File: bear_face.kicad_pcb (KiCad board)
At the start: 2 copper layers, 301.7 x 112.6 mm, 190 parts, among them J1 USB_B_Micro, SW1 SW_Push, U1 ATmega32U4-AU, Y1 16MHz

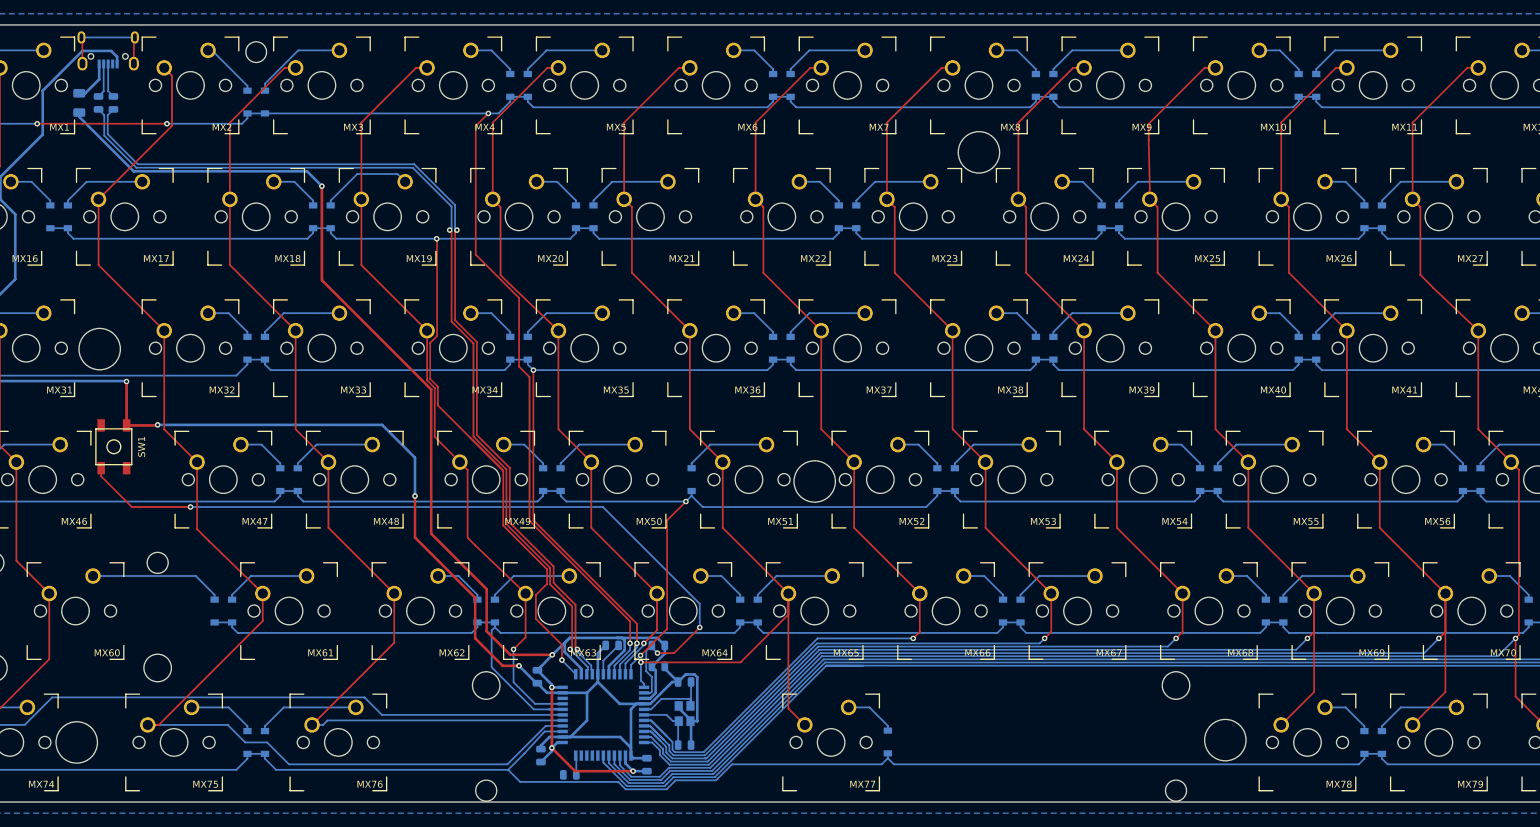
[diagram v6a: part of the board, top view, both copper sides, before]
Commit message: Load caps moved closer, minor MCU track tweaks, USB-Micro changed to molex
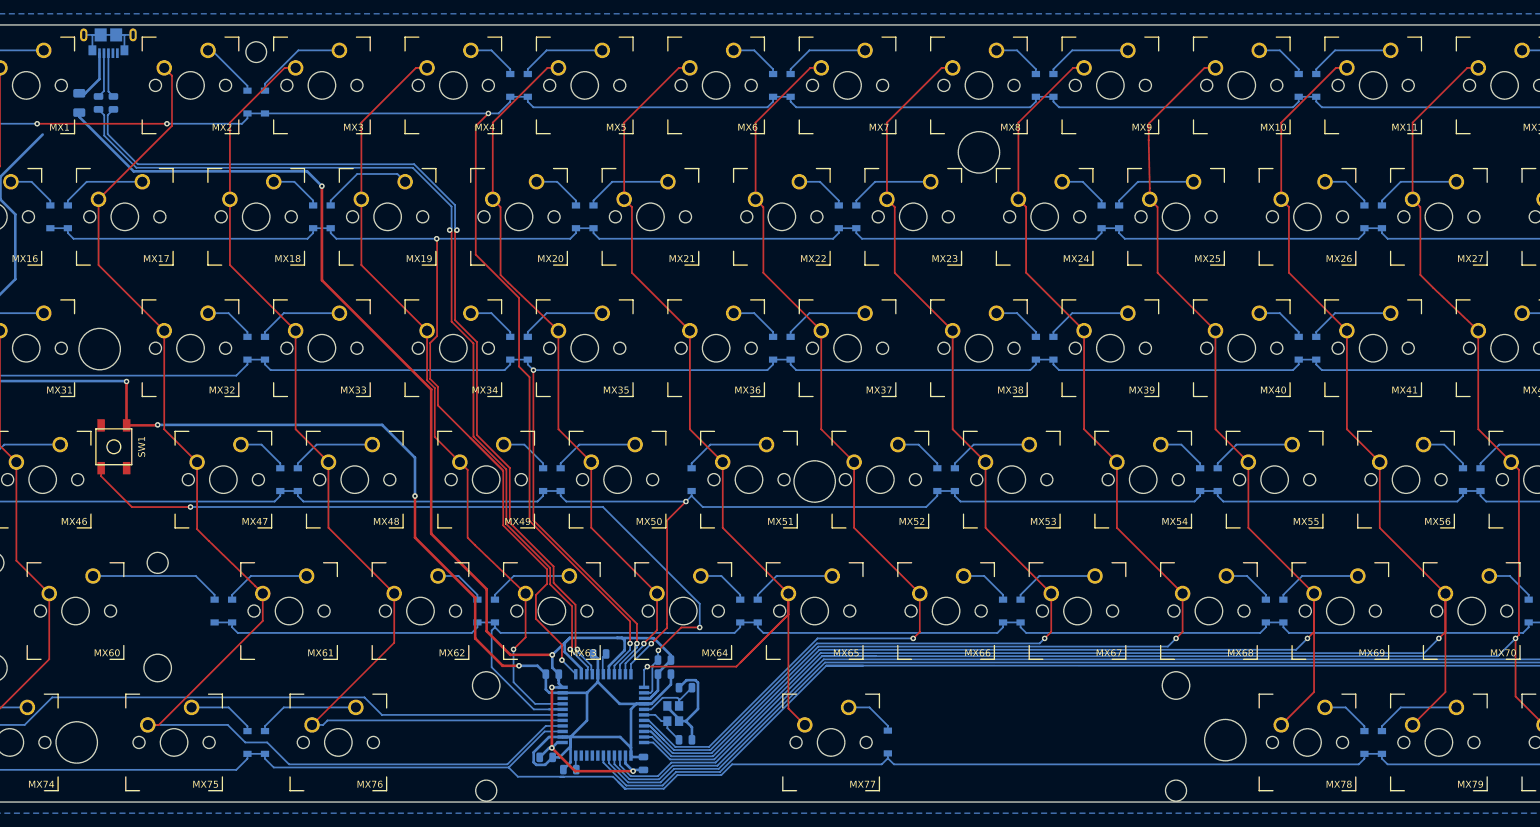
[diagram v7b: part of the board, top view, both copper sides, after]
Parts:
- J1: footprint Connector_USB:USB_Micro-B_Wuerth_629105150521 -> Connector_USB:USB_Micro-B_GCT_USB3076-30-A
- moved R1 2.31 mm to (164.7, 161.2)
- moved C3 2.19 mm to (155.3, 160.3)
- moved C7 2.19 mm to (148.5, 163.2), turned to 180 degrees
- moved Y1 1.65 mm to (166.0, 168.9)
- moved C5 1.42 mm to (164.7, 163.2)
- moved J1 1.12 mm to (84.1, 71.7)
- moved C2 0.84 mm to (167.8, 165.2)
- moved C6 0.80 mm to (147.6, 175.3), turned to 0 degrees
- moved C1 0.77 mm to (167.8, 172.7)
- moved R4 0.76 mm to (151.0, 177.0)
- moved C4 0.54 mm to (161.7, 176.1)
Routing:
- net COL5: track 142.1 -> 150.6 mm
- net GND: track 262.3 -> 253.8 mm
- net COL11: track 248.8 -> 256.5 mm
- net COL6: track 149.5 -> 145.0 mm
- net Net-(R1-Pad2): track 116.8 -> 114.0 mm
- net Net-(C3-Pad1): track 5.09 -> 3.17 mm
- net Net-(J1-Pad6): track 15.7 -> 13.9 mm
- net Net-(C1-Pad1): track 8.91 -> 7.16 mm
- net ROW5: track 306.8 -> 308.5 mm
- net Net-(C2-Pad1): track 11.9 -> 10.2 mm
- net VCC: track 5.95 -> 7.54 mm
- net D-: track 5.02 -> 6.60 mm
- net D+: track 5.02 -> 6.57 mm
- net COL8: track 186.2 -> 185.1 mm
- net COL7: track 168.8 -> 167.7 mm
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
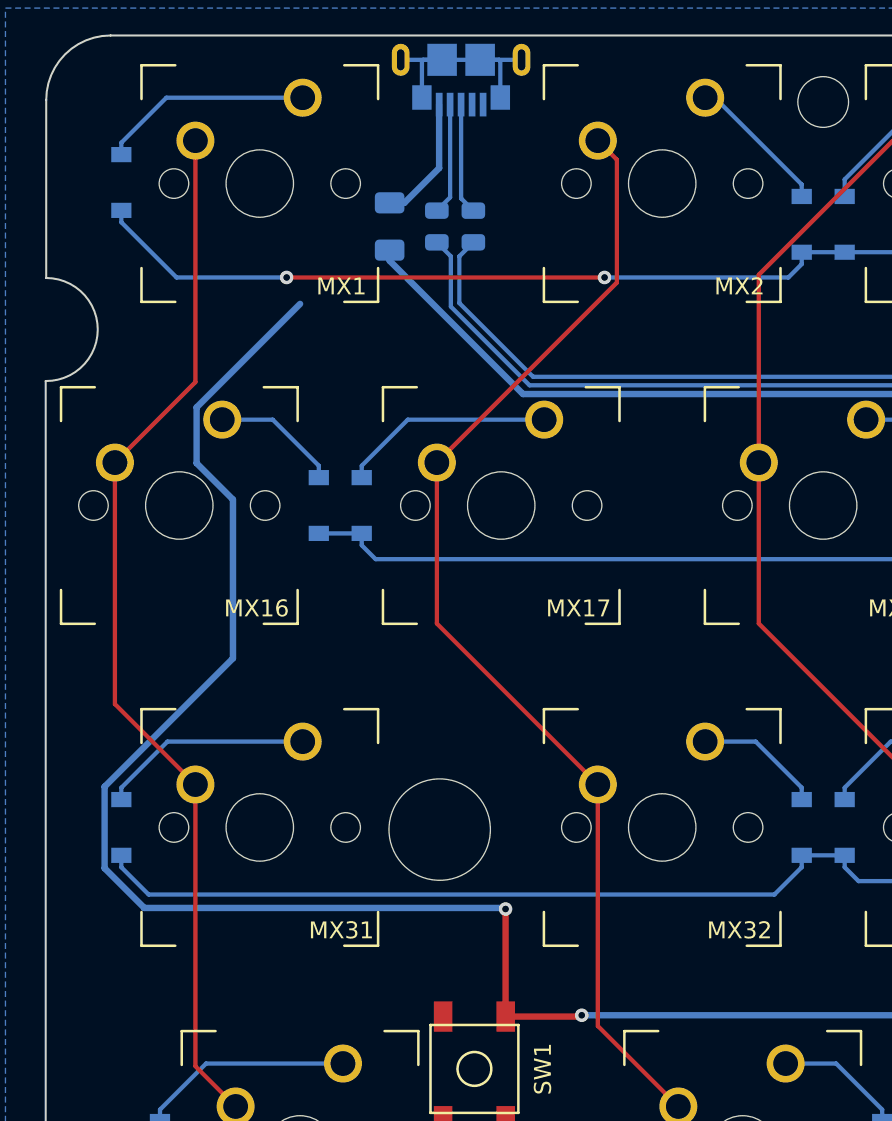
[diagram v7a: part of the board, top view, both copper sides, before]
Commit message: Reconnected USB GND to SW1
Minor tracking tweaks, DRC check passed
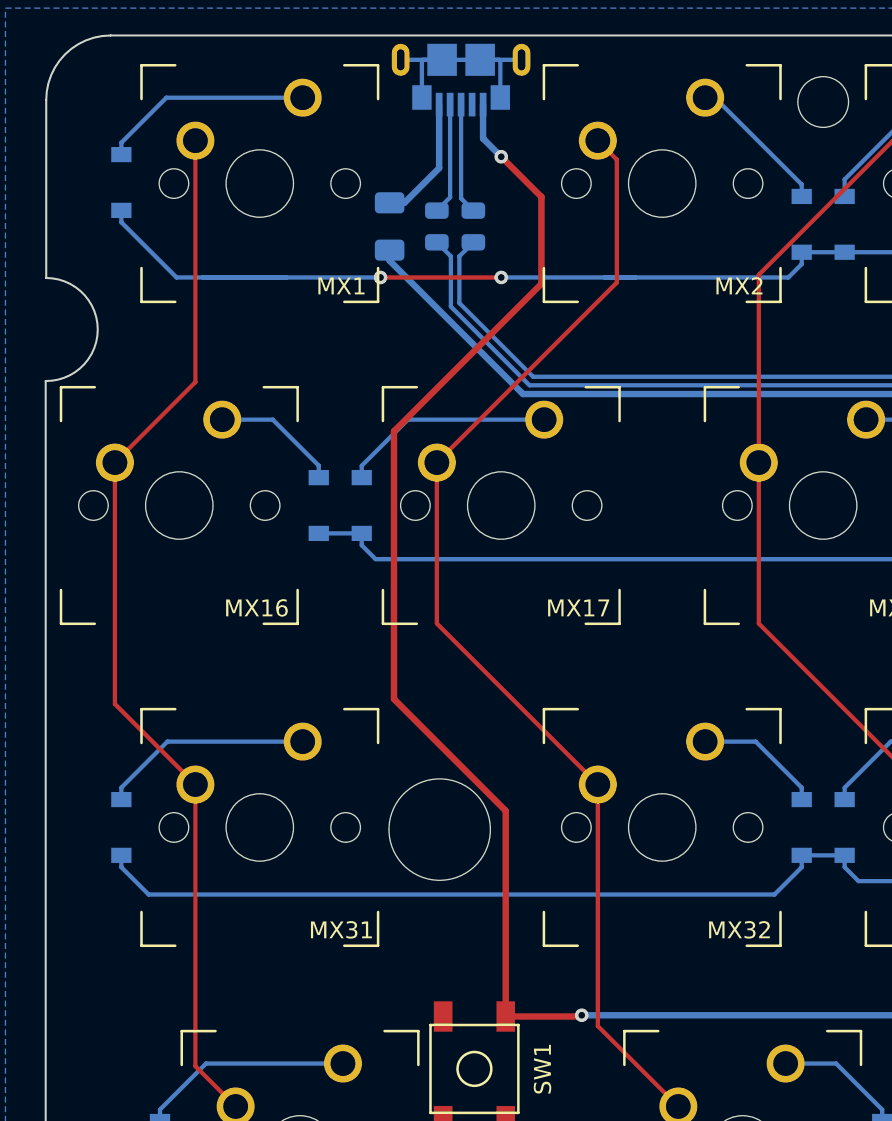
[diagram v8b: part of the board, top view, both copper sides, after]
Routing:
- net GND: track 253.8 -> 244.5 mm
- net ROW0: track 378.6 -> 385.4 mm
